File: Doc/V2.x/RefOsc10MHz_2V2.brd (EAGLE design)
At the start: 90 x 70 mm, 83 parts, among them CON1 TYCO-AMP_USBUSB-B_SMT, CON2 HEADER-2X5SMD, CON3 SD-73100-0105, CON4 AVR-ISP-6SMD, CON5 AVR-JTAG-10SMD, CON6 HEADER-2X3SMD, CON7 MCX-J-P-X-RA-SM1, IC1 ATmega328-P, IC2 LC4032V_XXT44, IC3 74HCT221D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

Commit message: avr_DF4IAH_Bootloader - Doc - Eagle: V2.2 - correction: CRS80 --> CRS08
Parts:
- D611, D921: value CRS80 -> CRS08
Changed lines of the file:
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@@
 <attribute name="VALUE" x="63.498440625" y="41.676578125" size="1.016" layer="27" rot="R180"/>
 </element>
-<element name="D611" library="diode" package="SOD80C" value="CRS80" x="53.34" y="45.72" smashed="yes" rot="MR270">
+<element name="D611" library="diode" package="SOD80C" value="CRS08" x="53.34" y="45.72" smashed="yes" rot="MR270">
 <attribute name="NAME" x="54.69835" y="43.927128125" size="1.016" layer="26" rot="MR90"/>
 <attribute name="VALUE" x="51.4271875" y="43.8820125" size="0.762" layer="28" rot="MR90"/>
 </element>
-<element name="D921" library="diode" package="SOD80C" value="CRS80" x="50.8" y="52.07" smashed="yes" rot="MR270">
+<element name="D921" library="diode" package="SOD80C" value="CRS08" x="50.8" y="52.07" smashed="yes" rot="MR270">
 <attribute name="NAME" x="50.984778125" y="55.33564375" size="1.016" layer="26" rot="MR90"/>
 <attribute name="VALUE" x="48.84568125" y="50.2119375" size="0.762" layer="28" rot="MR90"/>

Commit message: avr_DF4IAH_Bootloader - Doc - Eagle: V2.2 - correction: MCX socket ground not completed
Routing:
- net GND: track 336.4 -> 351.1 mm
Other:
- board text added: "DF4IAH 10 MHz Ref.-Osc. V 2.2a"
- board text removed: "DF4IAH 10 MHz Ref.-Osc. V 2.2"
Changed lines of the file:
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@@
 <text x="75.940734375" y="65.306415625" size="1.27" layer="26" font="vector" ratio="18" distance="61" rot="MR0" align="center-left">DF4IAH
 10 MHz Ref.-Osc.
-V 2.2</text>
+V 2.2a</text>
 <text x="6.35" y="10.16" size="1.27" layer="16" font="vector" ratio="20" distance="40" rot="MR0">Bot</text>
 <text x="2.54" y="10.16" size="1.27" layer="1" font="vector" ratio="20" distance="40">Top</text>
@@
 <wire x1="64.375" y1="49.25" x2="62" y2="49.25" width="0.508" layer="1"/>
 <wire x1="64.625" y1="49" x2="64.375" y2="49.25" width="0.508" layer="1"/>
-<wire x1="74.375" y1="49" x2="74" y2="49" width="0.508" layer="1"/>
-<wire x1="74" y1="49" x2="64.625" y2="49" width="0.508" layer="1"/>
+<wire x1="74.537021875" y1="49" x2="74" y2="49" width="0.508" layer="1"/>
+<wire x1="70.977334375" y1="49" x2="64.625" y2="49" width="0.508" layer="1"/>
 <wire x1="62" y1="49.25" x2="61.989234375" y2="49.347978125" width="0.508" layer="1"/>
 <wire x1="74" y1="49" x2="74" y2="40.64" width="0.508" layer="1"/>
@@
 <wire x1="76.479978125" y1="48.875" x2="76.91724375" y2="48.875" width="0.508" layer="1"/>
 <wire x1="76.91724375" y1="48.875" x2="83.5" y2="48.875" width="0.508" layer="1"/>
-<wire x1="74.5" y1="48.875" x2="74.375" y2="49" width="0.508" layer="1"/>
+<wire x1="74.5" y1="48.875" x2="74.537021875" y2="49" width="0.508" layer="1"/>
 <wire x1="23" y1="24.5" x2="21.875" y2="25.625" width="0.508" layer="1"/>
 <wire x1="28.125" y1="24.5" x2="25.625" y2="24.5" width="0.508" layer="1"/>
@@
 <via x="67.111434375" y="48.332225" extent="1-16" drill="0.35"/>
 <via x="64.135928125" y="48.627121875" extent="1-16" drill="0.35"/>
-<wire x1="81.24846875" y1="48.1757" x2="81.24846875" y2="48.789634375" width="0.508" layer="1"/>
-<wire x1="89.2271" y1="51.245365625" x2="88.811925" y2="51.245365625" width="0.508" layer="1"/>
+<wire x1="81.24846875" y1="48.1757" x2="81.24846875" y2="48.885025" width="0.508" layer="1"/>
 <wire x1="64.135928125" y1="48.645178125" x2="64.153978125" y2="48.645178125" width="0.508" layer="1"/>
 <wire x1="64.153978125" y1="48.645178125" x2="64.153978125" y2="49" width="0.508" layer="1"/>
@@
 <wire x1="67.114375" y1="48.5" x2="67.114375" y2="48.87991875" width="0.508" layer="1"/>
 <wire x1="70.977334375" y1="48.35626875" x2="70.977334375" y2="48.75" width="0.508" layer="1"/>
-<wire x1="70.977334375" y1="48.75" x2="70.977334375" y2="48.91603125" width="0.508" layer="1"/>
-<wire x1="74.533421875" y1="48.500725" x2="74.58743125" y2="49.015921875" width="0.508" layer="1"/>
+<wire x1="70.977334375" y1="48.75" x2="70.977334375" y2="49" width="0.508" layer="1"/>
+<wire x1="74.533421875" y1="48.500725" x2="74.533421875" y2="49.00691875" width="0.508" layer="1"/>
 <wire x1="85.616859375" y1="54.423375" x2="85.18363125" y2="54.423375" width="0.508" layer="1"/>
 <wire x1="85.18363125" y1="54.423375" x2="85.18363125" y2="54.25" width="0.508" layer="1"/>
@@
 <wire x1="61.148459375" y1="58.9978375" x2="61" y2="59.25" width="0.508" layer="1"/>
 <wire x1="77.811303125" y1="59.9970625" x2="77.75" y2="60" width="0.508" layer="1"/>
-<wire x1="74.75" y1="49" x2="74.58743125" y2="49.015921875" width="0.508" layer="1"/>
-<wire x1="74.75" y1="49" x2="74.75" y2="48.875" width="0.508" layer="1"/>
-<wire x1="83.5" y1="48.75" x2="83.700803125" y2="48.727109375" width="0.508" layer="1"/>
-<wire x1="83.5" y1="48.75" x2="83.5" y2="48.875" width="0.508" layer="1"/>
+<wire x1="76.190178125" y1="48.999996875" x2="74.533421875" y2="49.00691875" width="0.508" layer="1"/>
+<wire x1="76.190178125" y1="48.999996875" x2="74.75" y2="48.875" width="0.508" layer="1"/>
+<wire x1="83.5" y1="48.885025" x2="83.700803125" y2="48.727109375" width="0.508" layer="1"/>
+<wire x1="83.5" y1="48.885025" x2="83.5" y2="48.875" width="0.508" layer="1"/>
 <wire x1="83.75" y1="54" x2="83.700803125" y2="53.807109375" width="0.508" layer="1"/>
 <wire x1="83.75" y1="54" x2="83.75" y2="53.89305625" width="0.508" layer="1"/>
 <wire x1="88.75" y1="51" x2="88.75" y2="48.75" width="0.508" layer="1"/>
 <wire x1="88.75" y1="48.75" x2="88.780803125" y2="48.727109375" width="0.508" layer="1"/>
-<wire x1="88.75" y1="51" x2="88.811925" y2="51.245365625" width="0.508" layer="1"/>
+<wire x1="88.75" y1="51" x2="88.74988125" y2="51.2461375" width="0.508" layer="1"/>
+<wire x1="88.74988125" y1="51.2461375" x2="88.74891875" y2="53.24823125" width="0.508" layer="1"/>
 <wire x1="88.75" y1="54" x2="88.780803125" y2="53.807109375" width="0.508" layer="1"/>
 <wire x1="88.75" y1="54" x2="88.75" y2="53.89305625" width="0.508" layer="1"/>
@@
 <wire x1="67.114375" y1="48.32015625" x2="67.114375" y2="48.329284375" width="0.508" layer="1"/>
 <wire x1="67.114375" y1="48.329284375" x2="67.111434375" y2="48.332225" width="0.508" layer="1"/>
+<wire x1="89.2271" y1="51.245365625" x2="88.74988125" y2="51.245365625" width="0.508" layer="1"/>
+<wire x1="88.74988125" y1="51.245365625" x2="88.74988125" y2="51.2461375" width="0.508" layer="1"/>
+<wire x1="86.25169375" y1="48.061375" x2="86.248946875" y2="48.061375" width="0.508" layer="1"/>
+<wire x1="86.248946875" y1="48.061375" x2="86.248946875" y2="48.482859375" width="0.508" layer="1"/>
+<wire x1="88.780803125" y1="48.50558125" x2="86.25169375" y2="48.50558125" width="0.508" layer="1"/>
+<wire x1="83.807865625" y1="48.50558125" x2="83.825875" y2="48.721721875" width="0.508" layer="1"/>
+<wire x1="83.807865625" y1="48.50558125" x2="86.25169375" y2="48.50558125" width="0.508" layer="1"/>
+<wire x1="86.25169375" y1="48.50558125" x2="86.25169375" y2="48.061375" width="0.508" layer="1"/>
+<wire x1="88.780803125" y1="48.50558125" x2="88.780803125" y2="48.727109375" width="0.508" layer="1"/>
+<wire x1="83.825875" y1="48.721721875" x2="83.700803125" y2="48.721721875" width="0.508" layer="1"/>
+<wire x1="83.700803125" y1="48.721721875" x2="83.700803125" y2="48.727109375" width="0.508" layer="1"/>
+<wire x1="88.780803125" y1="53.807109375" x2="88.74891875" y2="53.807109375" width="0.508" layer="1"/>
+<wire x1="88.74891875" y1="53.807109375" x2="88.74891875" y2="53.24823125" width="0.508" layer="1"/>
+<wire x1="83.5" y1="48.885025" x2="81.24846875" y2="48.885025" width="0.508" layer="1"/>
+<wire x1="74" y1="49" x2="70.977334375" y2="49" width="0.508" layer="1"/>
+<wire x1="64.153978125" y1="49.11465625" x2="64.375" y2="49.11465625" width="0.508" layer="1"/>
+<wire x1="64.375" y1="49.11465625" x2="64.375" y2="49.25" width="0.508" layer="1"/>
 </signal>
 <signal name="VCC" class="2">

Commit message: avr_DF4IAH_Bootloader - Doc - Eagle: V2.1/V2.2 - removed elkos and replaced it by C0805 MLCCs
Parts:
- C151, C211, C612, C613: device rcl:PANASONIC_B -> rcl:C0805
- C911: device rcl:PANASONIC_C -> rcl:C0805
- moved C151 1.27 mm to (30.5, 19.1), turned to 180 degrees
- moved C911 1.27 mm to (24.1, 19.1), turned to 0 degrees
- turned C211 to 0 degrees
- turned C612 to 0 degrees
- turned C613 to 0 degrees
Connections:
- net +3V3: now also C612.1, C613.1; no longer C612.+, C613.+
- net GND: now also C151.2, C211.2, C612.2, C613.2, C911.2; no longer C151.-, C211.-, C612.-, C613.-, C911.-
- net N_ADC_PULL: now also C151.1; no longer C151.+
- net VCC: now also C211.1, C911.1; no longer C211.+, C911.+
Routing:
- net GND: track 351.1 -> 341.0 mm, vias 43 -> 44
- net VCC: track 297.6 -> 294.0 mm
- net N_ADC_PULL: track 75.6 -> 77.4 mm

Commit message: avr_DF4IAH_Bootloader - Doc - Eagle: 2.1, 2.2, 2.3 - three resistors changed
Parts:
- R311: value 4.7k -> 4.3k
- R611: value 10k -> 15k
- R612: value 45.3k -> 68k
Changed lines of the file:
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@@
 <attribute name="VALUE" x="29.21" y="16.51" size="1.016" layer="27"/>
 </element>
-<element name="R612" library="rcl" package="R0805" value="45.3k" x="46.99" y="40.64" smashed="yes" rot="MR0">
+<element name="R612" library="rcl" package="R0805" value="68k" x="46.99" y="40.64" smashed="yes" rot="MR0">
 <attribute name="NAME" x="45.007865625" y="39.54715625" size="1.016" layer="26" rot="MR180"/>
 <attribute name="VALUE" x="44.79206875" y="42.89283125" size="1.016" layer="28" rot="MR180"/>
 </element>
-<element name="R611" library="rcl" package="R0805" value="10k" x="48.26" y="46.99" smashed="yes" rot="MR90">
+<element name="R611" library="rcl" package="R0805" value="15k" x="48.26" y="46.99" smashed="yes" rot="MR90">
 <attribute name="NAME" x="49.2640875" y="45.7731" size="1.016" layer="26" rot="MR90"/>
 <attribute name="VALUE" x="47.568125" y="48.503196875" size="1.016" layer="28" rot="MR90"/>
@@
 <attribute name="VALUE" x="33.287240625" y="43.547825" size="1.016" layer="27" rot="R90"/>
 </element>
-<element name="R311" library="rcl" package="R0805" value="4.7k" x="20.32" y="11.43" smashed="yes" rot="MR0">
+<element name="R311" library="rcl" package="R0805" value="4.3k" x="20.32" y="11.43" smashed="yes" rot="MR0">
 <attribute name="NAME" x="25.05265625" y="10.7852375" size="1.016" layer="26" rot="MR0"/>
 <attribute name="VALUE" x="18.59439375" y="10.671171875" size="1.016" layer="28" rot="MR0"/>

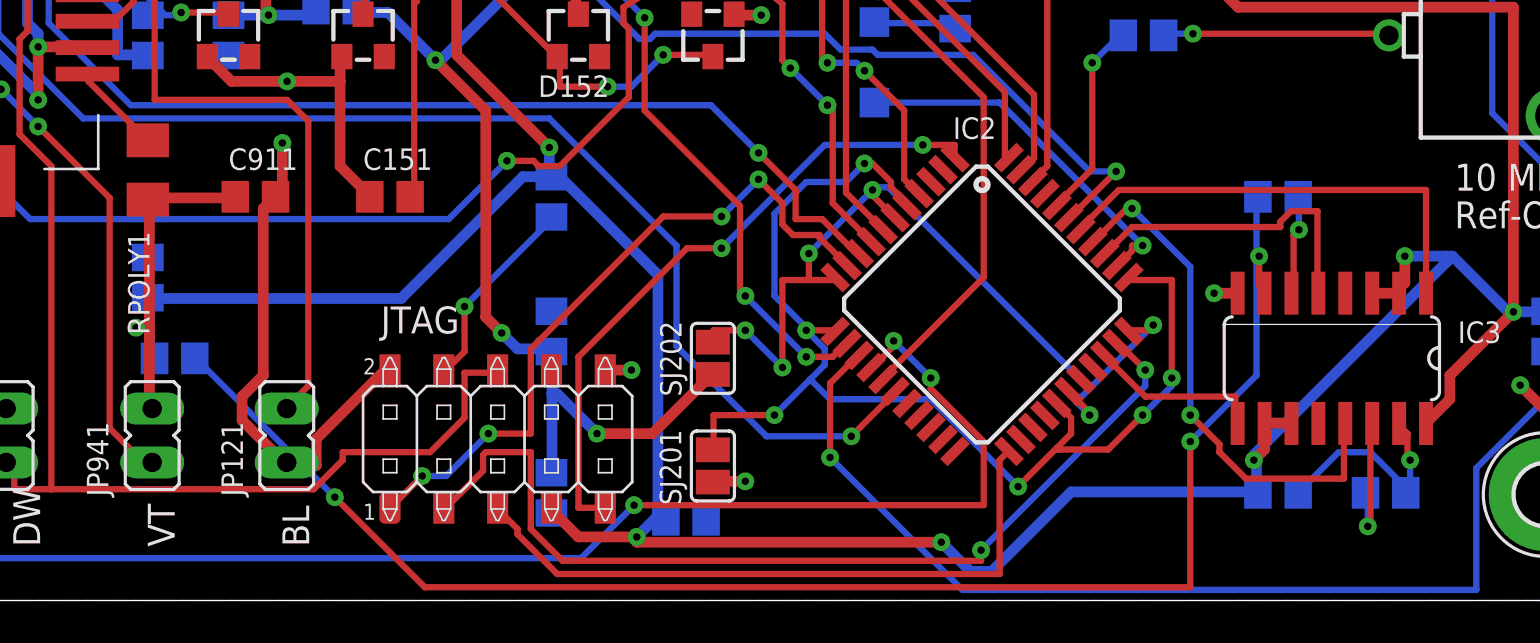
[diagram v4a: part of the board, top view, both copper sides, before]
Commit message: avr_DF4IAH_Bootloader - Doc - Eagle: 2.1, 2.2, 2.3 - misplaced R311 fixed (making short at BL jumper)
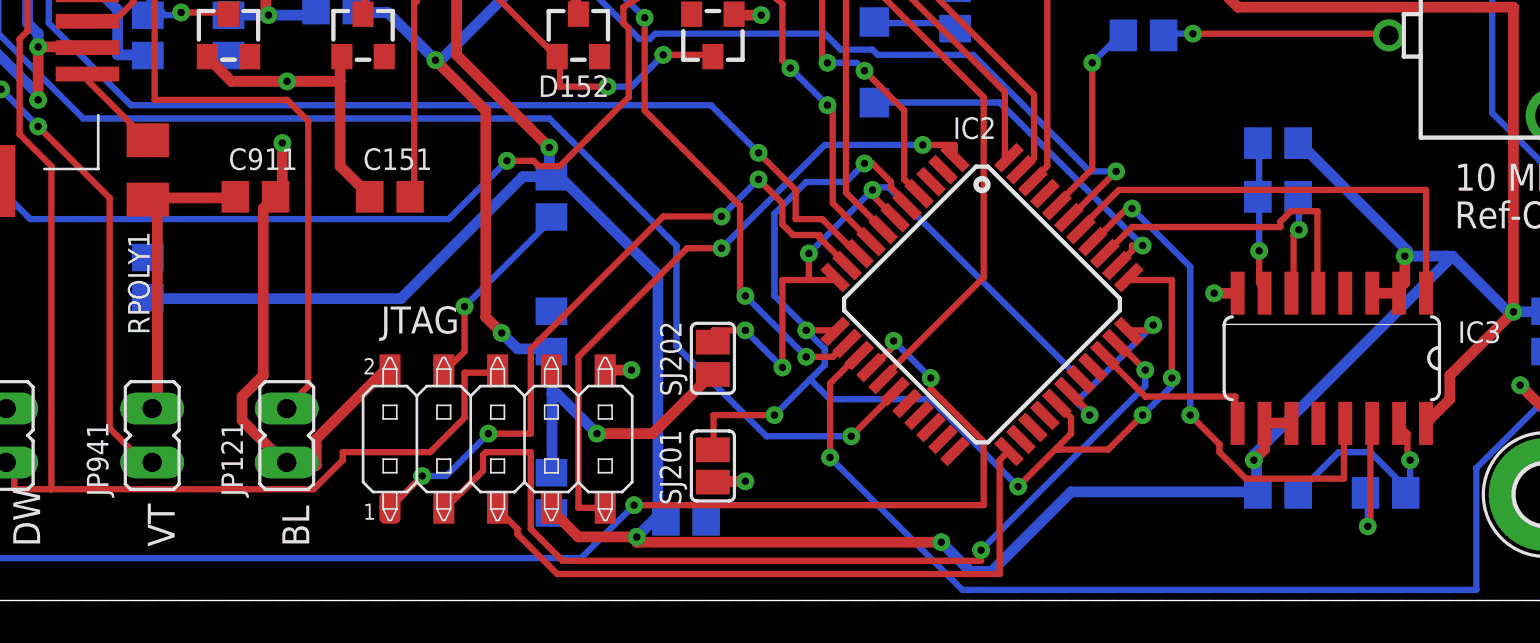
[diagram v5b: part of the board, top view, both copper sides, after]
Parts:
- moved R311 53.1 mm to (72.4, 21.6), turned to 180 degrees
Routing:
- net N$44: track 73.2 -> 7.20 mm, vias 3 -> 1
- net VCC: track 294.0 -> 302.7 mm, vias 11 -> 10
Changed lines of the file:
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@@
 <attribute name="VALUE" x="33.287240625" y="43.547825" size="1.016" layer="27" rot="R90"/>
 </element>
-<element name="R311" library="rcl" package="R0805" value="4.3k" x="20.32" y="11.43" smashed="yes" rot="MR0">
-<attribute name="NAME" x="25.05265625" y="10.7852375" size="1.016" layer="26" rot="MR0"/>
-<attribute name="VALUE" x="18.59439375" y="10.671171875" size="1.016" layer="28" rot="MR0"/>
+<element name="R311" library="rcl" package="R0805" value="4.3k" x="72.39" y="21.59" smashed="yes" rot="MR180">
+<attribute name="NAME" x="75.018709375" y="21.87325" size="1.016" layer="26" rot="MR180"/>
+<attribute name="VALUE" x="66.82648125" y="22.131921875" size="1.016" layer="28" rot="MR180"/>
 </element>
 <element name="C612" library="rcl" package="C0805" value="22uF" x="43.18" y="39.37" smashed="yes">
@@
 <wire x1="83.5" y1="28" x2="70.5" y2="28" width="0.508" layer="1"/>
 <wire x1="83.5" y1="13.625" x2="83.5" y2="28" width="0.508" layer="1"/>
-<wire x1="19.125" y1="11.625" x2="19.125" y2="12.875" width="0.508" layer="16"/>
-<wire x1="19.125" y1="12.875" x2="19.125" y2="14.25" width="0.508" layer="16"/>
-<wire x1="19.25" y1="11.5" x2="19.125" y2="11.625" width="0.508" layer="16"/>
-<wire x1="19.125" y1="14.25" x2="19.05" y2="14.29" width="0.508" layer="16"/>
-<wire x1="19.25" y1="11.5" x2="19.37" y2="11.43" width="0.508" layer="16"/>
 <wire x1="19.125" y1="19" x2="19.05" y2="18.92" width="0.508" layer="1"/>
-<wire x1="19.125" y1="18.75" x2="19.125" y2="12.875" width="0.508" layer="1"/>
-<wire x1="19.125" y1="12.875" x2="19.125" y2="9.25" width="0.508" layer="1"/>
-<wire x1="19.125" y1="9.25" x2="19.125" y2="9" width="0.508" layer="1"/>
-<wire x1="19.125" y1="18.75" x2="19.05" y2="18.92" width="0.508" layer="1"/>
-<wire x1="18.5" y1="12.875" x2="19.125" y2="12.875" width="0.508" layer="16"/>
-<wire x1="19.125" y1="12.875" x2="18.5" y2="12.875" width="0.508" layer="1"/>
 <wire x1="41.75" y1="50" x2="42.125" y2="49.625" width="0.508" layer="1"/>
 <wire x1="41.75" y1="53.25" x2="41.75" y2="50" width="0.508" layer="1"/>
@@
 <via x="83.5" y="13.625" extent="1-16" drill="0.35"/>
 <via x="78.375" y="16.25" extent="1-16" drill="0.35"/>
-<via x="18.5" y="12.875" extent="1-16" drill="0.35"/>
 <via x="39.75" y="58.125" extent="1-16" drill="0.35"/>
 <via x="42.125" y="3" extent="1-16" drill="0.35"/>
@@
 <wire x1="41.75" y1="53.25" x2="41.5" y2="53.5" width="0.508" layer="1"/>
 <contactref element="JP941" pad="1"/>
-<wire x1="19.25" y1="9.25" x2="19.25806875" y2="9.05663125" width="0.508" layer="1"/>
-<wire x1="19.25" y1="9.25" x2="19.125" y2="9.25" width="0.508" layer="1"/>
 <wire x1="19.375" y1="19" x2="23.125" y2="19" width="0.508" layer="1"/>
 <wire x1="23.125" y1="19" x2="23.18" y2="19.05" width="0.508" layer="1"/>
@@
 <wire x1="41.5" y1="54.625" x2="42.125" y2="54.625" width="0.508" layer="1"/>
 <wire x1="42.125" y1="54.625" x2="42.23" y2="54.61" width="0.508" layer="1"/>
+<wire x1="78.5" y1="16.5" x2="73.5" y2="21.5" width="0.508" layer="16"/>
+<wire x1="73.5" y1="21.5" x2="73.34" y2="21.59" width="0.508" layer="16"/>
+<wire x1="78.5" y1="16.5" x2="78.375" y2="16.25" width="0.508" layer="16"/>
+<wire x1="19.5" y1="14" x2="19.5" y2="9.5" width="0.508" layer="16"/>
+<wire x1="19.5" y1="9.5" x2="19.25806875" y2="9.05663125" width="0.508" layer="16"/>
+<wire x1="19.5" y1="14" x2="19.05" y2="14.29" width="0.508" layer="16"/>
+<wire x1="19.5" y1="9.5" x2="19.5" y2="18.5" width="0.508" layer="1"/>
+<wire x1="19.5" y1="18.5" x2="19.05" y2="18.92" width="0.508" layer="1"/>
+<wire x1="19.5" y1="9.5" x2="19.25806875" y2="9.05663125" width="0.508" layer="1"/>
 </signal>
 <signal name="N_ADC_PULL">
@@
 <contactref element="C311" pad="2"/>
 <contactref element="R311" pad="1"/>
-<wire x1="27.875" y1="4.875" x2="21.375" y2="11.375" width="0.3" layer="16"/>
-<wire x1="32.125" y1="0.625" x2="27.875" y2="4.875" width="0.3" layer="1"/>
-<wire x1="68.25" y1="0.625" x2="32.125" y2="0.625" width="0.3" layer="1"/>
-<wire x1="68.25" y1="7.5" x2="68.25" y2="0.625" width="0.3" layer="1"/>
-<wire x1="71.375" y1="10.625" x2="68.25" y2="7.5" width="0.3" layer="16"/>
-<wire x1="71.375" y1="19" x2="71.375" y2="16.25" width="0.3" layer="16"/>
-<wire x1="71.375" y1="16.25" x2="71.375" y2="10.625" width="0.3" layer="16"/>
-<wire x1="21.375" y1="11.375" x2="21.27" y2="11.43" width="0.3" layer="16"/>
-<wire x1="71.375" y1="19" x2="71.44" y2="19.05" width="0.3" layer="16"/>
-<wire x1="71.5" y1="14.875" x2="71.75" y2="14.625" width="0.3" layer="1"/>
-<wire x1="71.5" y1="16.25" x2="71.5" y2="14.875" width="0.3" layer="1"/>
-<wire x1="71.75" y1="14.625" x2="71.755" y2="14.5034" width="0.3" layer="1"/>
-<wire x1="71.5" y1="16.25" x2="71.375" y2="16.25" width="0.3" layer="16"/>
-<via x="27.875" y="4.875" extent="1-16" drill="0.35"/>
-<via x="68.25" y="7.5" extent="1-16" drill="0.35"/>
-<via x="71.5" y="16.25" extent="1-16" drill="0.35"/>
+<wire x1="71.5" y1="21.5" x2="71.5" y2="19.5" width="0.3" layer="16"/>
+<wire x1="71.5" y1="19.5" x2="71.44" y2="19.05" width="0.3" layer="16"/>
+<wire x1="71.5" y1="21.5" x2="71.44" y2="21.59" width="0.3" layer="16"/>
+<wire x1="71.5" y1="16.5" x2="71.5" y2="15" width="0.3" layer="1"/>
+<wire x1="71.5" y1="19" x2="71.5" y2="16.5" width="0.3" layer="16"/>
+<wire x1="71.5" y1="15" x2="71.755" y2="14.5034" width="0.3" layer="1"/>
+<wire x1="71.5" y1="19" x2="71.44" y2="19.05" width="0.3" layer="16"/>
+<via x="71.5" y="16.5" extent="1-16" drill="0.35"/>
 </signal>
 <signal name="N$45">
